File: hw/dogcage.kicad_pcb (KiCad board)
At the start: 2 copper layers, 68.6 x 49.8 mm, 17 parts, among them CON1 5V, M1 XBee, P1 Door, P2 Servo, P3 CONN_01X10, P4 CONN_01X10, P5 CONN_01X14, P7 CONN_01X14, Q1 TIP120, SW1 Trigger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

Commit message: Placement in progress
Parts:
- removed M1: XBee, modules:xbee
- removed P3, P4: CONN_01X10, Pin_Headers:Pin_Header_Straight_1x10
- removed P5, P7: CONN_01X14, Pin_Headers:Pin_Header_Straight_1x14
- added C3: 10uF, Capacitors_SMD:C_0805_HandSoldering, F.Cu at (170.2, 170.9)
- added C4: 100uF, Capacitors_SMD:c_elec_3x5.3, F.Cu at (156.2, 161.8)
- added Q2: TIP120, Power_Integrations:TO-220, F.Cu at (166.6, 158.5)
- added R2: 10K, Resistors_SMD:R_0805_HandSoldering, F.Cu at (190.6, 134.1)
- added R3: 330, Resistors_SMD:R_0805_HandSoldering, F.Cu at (190.8, 124.3)
- added R4: 10K, Resistors_SMD:R_0805_HandSoldering, F.Cu at (190.8, 131.0)
- added R5: 470, Resistors_SMD:R_0805_HandSoldering, F.Cu at (170.2, 162.8)
- added R6: 470, Resistors_SMD:R_0805_HandSoldering, F.Cu at (170.2, 165.6)
- added SW2: SW_PUSH, Buttons_Switches_ThroughHole:SW_PUSH_SMALL, F.Cu at (153.4, 136.9)
- added U3: TEENSYLC, modules:Teensy-3.1, F.Cu at (192.2, 137.8)
- added U4: ESP-01v090, ESP8266:ESP-01, F.Cu at (184.7, 130.8)
- C1: value 10uF -> .1uF; footprint Capacitors_Elko_ThroughHole:Elko_vert_11x5mm_RM2 -> Capacitors_SMD:C_0805_HandSoldering
- C2: footprint Capacitors_Elko_ThroughHole:Elko_vert_11x5mm_RM2 -> Capacitors_SMD:C_0805_HandSoldering
- CON1: value 5V -> BARREL_JACK
- D1: value Assoc -> 1N4001; footprint LEDs:LED-3MM -> Diodes_ThroughHole:Diode_DO-41_SOD81_Horizontal_RM10
- D2: value 1N4001 -> Assoc LED; footprint Diodes_ThroughHole:Diode_DO-41_SOD81_Horizontal_RM10 -> LEDs:LED-0805
- P1: footprint Pin_Headers:Pin_Header_Straight_1x02 -> Pin_Headers:Pin_Header_Straight_1x03
- P2: value Servo -> Lock
- R1: value 330 -> 10K; footprint Resistors_ThroughHole:Resistor_Horizontal_RM10mm -> Resistors_SMD:R_0805_HandSoldering
- SW1: value Trigger -> SW_PUSH
- U1: value LD1117S33TR -> LD1117S50TR
- U2: value Teensy LC -> LD1117S33TR; footprint modules:Teensy-3.1 -> SMD_Packages:SOT-223
- moved U2 58.5 mm to (179.3, 171.2)
- moved SW1 49.2 mm to (153.1, 124.0), turned to 90 degrees
- moved D2 44.1 mm to (190.6, 120.7)
- moved R1 39.2 mm to (190.8, 128.2), turned to 180 degrees
- moved D1 32.1 mm to (186.2, 161.3), turned to 0 degrees
- moved P1 13.9 mm to (158.5, 167.9)
- moved C2 8.48 mm to (170.2, 173.5), turned to 180 degrees
- moved U1 6.61 mm to (179.3, 163.6)
- moved C1 4.50 mm to (170.2, 168.4), turned to 180 degrees
- moved Q1 3.05 mm to (164.3, 168.9), turned to 90 degrees
- moved P2 2.05 mm to (153.2, 167.9)
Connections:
- C1 pad 1: +5V -> VCC
- C2 pad 1: +3V3 -> +5V
- CON1 pad 3: Net-(CON1-Pad3) -> (no net)
- D1 pad 1: GND -> VCC
- D1 pad 2: Net-(D1-Pad2) -> Net-(CON1-Pad1)
- D2 pad 1: +5V -> Net-(D2-Pad1)
- D2 pad 2: Net-(CON1-Pad1) -> +3V3
- P1 pad 1: Net-(P1-Pad1) -> /D175V
- P1 pad 2: GND -> +5V
- P2 pad 1: Net-(P2-Pad1) -> /D175V
- Q1 pad 2: Net-(P2-Pad3) -> Net-(P1-Pad3)
- R1 pad 1: Net-(M1-Pad15) -> +3V3
- R1 pad 2: Net-(D1-Pad2) -> /D2
- SW1 pad 1: Net-(P5-Pad13) -> /D10
- U1 pad 2: +3V3 -> +5V
- U1 pad 3: +5V -> VCC
- U2 pad 2: Net-(P5-Pad2) -> +3V3
- U2 pad 3: Net-(P5-Pad3) -> +5V
- U2 pad 4: Net-(P5-Pad4) -> (no net)
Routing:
- net +5V: track 93.8 -> 0.00 mm, vias 4 -> 0
- net GND: track 52.6 -> 0.00 mm, vias 6 -> 0
- net Net-(M1-Pad15): track 51.5 -> 0.00 mm, vias 2 -> 0
- net +3V3: track 47.9 -> 0.00 mm, vias 1 -> 0
- net Net-(P5-Pad13): track 20.7 -> 0.00 mm
- net /XBEE_CTL: track 19.9 -> 0.00 mm
- net Net-(P1-Pad1): track 16.6 -> 0.00 mm
- net Net-(P2-Pad1): track 14.8 -> 0.00 mm
- net Net-(Q1-Pad1): track 14.3 -> 0.00 mm
- net Net-(P2-Pad3): track 11.7 -> 0.00 mm
- net Net-(CON1-Pad1): track 8.23 -> 0.00 mm
- net Net-(M1-Pad20): track 5.55 -> 0.00 mm
- net Net-(M1-Pad2): track 5.33 -> 0.00 mm
- net Net-(M1-Pad19): track 5.33 -> 0.00 mm
- net Net-(M1-Pad3): track 5.10 -> 0.00 mm
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- removed copper zone on B.Cu, net GND

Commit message: Placement is essentially done
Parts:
- removed SW1: SW_PUSH, Buttons_Switches_ThroughHole:SW_PUSH_SMALL
- added Activate: SW_PUSH, Buttons_Switches_ThroughHole:SW_PUSH_SMALL, F.Cu at (164.1, 170.7)
- CON1: value BARREL_JACK -> 6.5V+; footprint Connect:BARREL_JACK -> modules:BARREL_JACK-ROUND_TH
- Q1, Q2: value TIP120 -> Darl_NPN; footprint Power_Integrations:TO-220 -> SMD_Packages:DPAK-2; moved to B.Cu
- R5, R6: moved to B.Cu
- SW2: footprint Buttons_Switches_ThroughHole:SW_PUSH_SMALL -> Buttons_Switches_SMD:SW_SPST_FSMSM
- U3: value TEENSYLC -> Teensy LC
- U4: value ESP-01v090 -> ESP8266
- moved SW2 41.8 mm to (195.1, 133.6), turned to 270 degrees
- moved C4 15.0 mm to (171.2, 163.1), turned to 90 degrees
- moved P2 10.8 mm to (161.5, 161.0), turned to 90 degrees
- moved Q1 10.1 mm to (174.2, 170.8)
- moved Q2 9.06 mm to (174.4, 163.2), turned to 90 degrees
- moved D2 6.83 mm to (190.0, 127.5)
- moved U4 6.65 mm to (182.9, 137.2)
- moved R3 6.28 mm to (190.0, 130.6)
- moved R4 5.67 mm to (190.0, 136.7), turned to 180 degrees
- moved R2 5.62 mm to (190.0, 139.7), turned to 180 degrees
- moved R1 5.43 mm to (190.0, 133.6)
- moved R6 4.85 mm to (170.7, 170.4), turned to 90 degrees
- moved U3 4.53 mm to (191.5, 142.2)
- moved P1 4.49 mm to (161.5, 164.6), turned to 90 degrees
- moved C1 1.27 mm to (171.2, 167.6)
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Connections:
- Q1 pad 1: Net-(Q1-Pad1) -> GND
- Q1 pad 2: Net-(P1-Pad3) -> Net-(Q1-Pad2)
- Q1 pad 3: GND -> Net-(P1-Pad3)
- Q2 pad 1: Net-(Q2-Pad1) -> GND
- Q2 pad 2: Net-(P2-Pad3) -> Net-(Q2-Pad2)
- Q2 pad 3: GND -> Net-(P2-Pad3)
- R5 pad 1: /D11 -> /D14
- R5 pad 2: Net-(Q1-Pad1) -> Net-(Q1-Pad2)
- R6 pad 1: /D12 -> /D15
- R6 pad 2: Net-(Q2-Pad1) -> Net-(Q2-Pad2)
- U3 pad 13: /D11 -> (no net)
- U3 pad 14: /D12 -> (no net)
- U3 pad 21: (no net) -> /D14
- U3 pad 22: (no net) -> /D15
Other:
- board size 68.6 x 49.8 mm -> 40.6 x 49.8 mm
- board text added: "Tom Manley tom.manley@gmail.com https://github.com/tpmanley/dogcage Version 2.0"
- board text removed: "https://github.com/tpmanley/dogcage Tom Manley tom.manley@gmail.com"

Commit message: Partially routed
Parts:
- removed Activate: SW_PUSH, Buttons_Switches_ThroughHole:SW_PUSH_SMALL
- added SW1: Activate, Buttons_Switches_ThroughHole:SW_PUSH_SMALL, F.Cu at (163.8, 170.9)
- moved R1 5.59 mm to (190.0, 139.2)
- moved R2 3.30 mm to (190.0, 136.4)
- moved R4 2.79 mm to (190.0, 133.9)
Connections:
- U3 pad 12: /D10 -> (no net)
- U3 pad 19: (no net) -> Net-(SW1-Pad2)
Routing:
- net +3V3: track 0.00 -> 97.9 mm, vias 0 -> 4
- net +5V: track 0.00 -> 41.1 mm, vias 0 -> 1
- net /TX1: track 0.00 -> 24.1 mm
- net Net-(CON1-Pad1): track 0.00 -> 22.9 mm
- net /D175V: track 0.00 -> 22.2 mm
- net VCC: track 0.00 -> 21.7 mm
- net /D2: track 0.00 -> 19.2 mm
- net Net-(R3-Pad2): track 0.00 -> 17.1 mm
- net Net-(SW1-Pad2): track 0.00 -> 14.7 mm
- net /RX1: track 0.00 -> 12.2 mm
- net Net-(R4-Pad2): track 0.00 -> 6.50 mm
- net Net-(R2-Pad2): track 0.00 -> 6.50 mm
- net Net-(D2-Pad1): track 0.00 -> 3.17 mm
- net Net-(P1-Pad3): track 0.00 -> 1.40 mm
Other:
- net class Power added: clearance 0.2, trace_width 0.762, via_dia 0.6858, via_drill 0.3302

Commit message: More routing
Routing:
- net +5V: track 41.1 -> 47.7 mm
- net Net-(P1-Pad3): track 1.40 -> 3.84 mm
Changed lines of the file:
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@@
   (general
     (links 49)
-    (no_connects 24)
+    (no_connects 23)
     (area 155.19281 124.351 201.577621 175.310001)
     (thickness 1.6)
     (drawings 5)
-    (tracks 100)
+    (tracks 108)
     (zones 0)
     (modules 23)
@@
     (pad_to_mask_clearance 0)
     (aux_axis_origin 0 0)
-    (visible_elements FFFF7B7F)
+    (visible_elements FFFFFF7F)
     (pcbplotparams
       (layerselection 0x010f0_80000001)
@@
   )
   (gr_line (start 198.12 125.476) (end 198.12 175.26) (angle 90) (layer Edge.Cuts) (width 0.1))
-  (segment (start 171.196 161.56686) (end 171.196 160.274) (width 0.762) (layer F.Cu) (net 1))
-  (segment (start 171.196 160.274) (end 171.196 159.258) (width 0.762) (layer B.Cu) (net 1))
-  (via (at 171.196 160.274) (size 0.6858) (layers F.Cu B.Cu) (net 1))
+  (segment (start 171.196 161.56686) (end 171.196 161.544) (width 0.508) (layer F.Cu) (net 1))
+  (segment (start 171.196 161.544) (end 169.799 160.147) (width 0.508) (layer F.Cu) (net 1))
+  (segment (start 169.799 160.147) (end 169.799 159.004) (width 0.508) (layer B.Cu) (net 1))
+  (via (at 169.799 160.147) (size 0.6858) (layers F.Cu B.Cu) (net 1))
+  (segment (start 168.656 159.004) (end 169.799 159.004) (width 0.508) (layer B.Cu) (net 1))
+  (segment (start 169.799 159.004) (end 192.532 159.004) (width 0.508) (layer B.Cu) (net 1))
+  (segment (start 192.532 159.004) (end 194.056 157.48) (width 0.508) (layer B.Cu) (net 1))
+  (segment (start 166.116 159.004) (end 164.084 161.036) (width 0.508) (layer B.Cu) (net 1))
+  (segment (start 168.656 159.004) (end 166.116 159.004) (width 0.508) (layer B.Cu) (net 1))
+  (segment (start 171.196 161.56686) (end 172.99686 161.56686) (width 0.762) (layer F.Cu) (net 1))
+  (segment (start 172.99686 161.56686) (end 175.006 163.576) (width 0.762) (layer F.Cu) (net 1))
+  (segment (start 175.006 163.576) (end 176.022 163.576) (width 0.762) (layer F.Cu) (net 1))
   (segment (start 164.084 161.036) (end 164.084 160.782) (width 0.762) (layer B.Cu) (net 1))
-  (segment (start 164.084 160.782) (end 165.608 159.258) (width 0.762) (layer B.Cu) (net 1))
-  (segment (start 192.278 159.258) (end 194.056 157.48) (width 0.762) (layer B.Cu) (net 1))
-  (segment (start 165.608 159.258) (end 171.196 159.258) (width 0.762) (layer B.Cu) (net 1))
-  (segment (start 171.196 159.258) (end 192.278 159.258) (width 0.762) (layer B.Cu) (net 1))
   (segment (start 164.084 161.036) (end 164.084 164.592) (width 0.762) (layer B.Cu) (net 1))
   (segment (start 172.7 173.482) (end 172.446 173.736) (width 0.762) (layer F.Cu) (net 1))
   (segment (start 176.022 173.482) (end 172.7 173.482) (width 0.762) (layer F.Cu) (net 1))
-  (segment (start 172.446 169.184) (end 169.184 169.184) (width 0.762) (layer F.Cu) (net 3))
+  (segment (start 172.446 169.184) (end 169.184 169.184) (width 0.508) (layer F.Cu) (net 3))
+  (segment (start 169.184 169.184) (end 169.164 169.164) (width 0.508) (layer F.Cu) (net 3))
+  (via (at 169.164 169.164) (size 0.6858) (layers F.Cu B.Cu) (net 3))
+  (segment (start 168.91 165.354) (end 168.91 166.116) (width 0.508) (layer F.Cu) (net 3))
+  (segment (start 168.91 159.258) (end 172.158002 159.258) (width 0.508) (layer F.Cu) (net 3))
+  (segment (start 175.768 159.258) (end 179.07 159.258) (width 0.508) (layer F.Cu) (net 3))
+  (segment (start 181.102 159.258) (end 183.134 159.258) (width 0.508) (layer F.Cu) (net 3))
+  (segment (start 184.912 159.258) (end 187.706 159.258) (width 0.508) (layer F.Cu) (net 3))
+  (segment (start 196.342 154.178) (end 196.342 159.258) (width 0.508) (layer F.Cu) (net 3))
+  (segment (start 192.532 139.192) (end 193.802 140.462) (width 0.508) (layer F.Cu) (net 3))
+  (segment (start 193.802 140.462) (end 195.072 140.462) (width 0.508) (layer F.Cu) (net 3))
+  (segment (start 195.072 140.462) (end 196.342 141.732) (width 0.508) (layer F.Cu) (net 3))
+  (segment (start 196.342 141.732) (end 196.342 154.178) (width 0.508) (layer F.Cu) (net 3))
+  (segment (start 192.532 139.192) (end 191.342 139.192) (width 0.508) (layer F.Cu) (net 3))
+  (segment (start 196.342 159.258) (end 189.484 159.258) (width 0.508) (layer F.Cu) (net 3))
+  (segment (start 187.706 159.258) (end 189.484 159.258) (width 0.508) (layer F.Cu) (net 3))
+  (segment (start 183.134 159.258) (end 184.912 159.258) (width 0.508) (layer F.Cu) (net 3))
+  (segment (start 179.07 159.258) (end 181.102 159.258) (width 0.508) (layer F.Cu) (net 3))
+  (segment (start 172.158002 159.258) (end 175.768 159.258) (width 0.508) (layer F.Cu) (net 3))
+  (segment (start 168.91 159.258) (end 168.91 165.354) (width 0.508) (layer F.Cu) (net 3))
+  (segment (start 169.164 166.37) (end 169.164 169.164) (width 0.508) (layer B.Cu) (net 3))
+  (segment (start 168.91 166.116) (end 169.164 166.37) (width 0.508) (layer B.Cu) (net 3))
   (via (at 168.91 166.116) (size 0.6858) (layers F.Cu B.Cu) (net 3))
-  (segment (start 168.91 166.116) (end 169.164 166.37) (width 0.762) (layer B.Cu) (net 3))
-  (segment (start 169.164 166.37) (end 169.164 169.164) (width 0.762) (layer B.Cu) (net 3))
-  (segment (start 168.91 159.258) (end 168.91 165.354) (width 0.762) (layer F.Cu) (net 3))
-  (segment (start 172.158002 159.258) (end 175.768 159.258) (width 0.762) (layer F.Cu) (net 3))
-  (segment (start 179.07 159.258) (end 181.102 159.258) (width 0.762) (layer F.Cu) (net 3))
-  (segment (start 183.134 159.258) (end 184.912 159.258) (width 0.762) (layer F.Cu) (net 3))
-  (segment (start 187.706 159.258) (end 189.484 159.258) (width 0.762) (layer F.Cu) (net 3))
-  (segment (start 196.342 159.258) (end 189.484 159.258) (width 0.762) (layer F.Cu) (net 3))
-  (segment (start 192.532 139.192) (end 191.342 139.192) (width 0.762) (layer F.Cu) (net 3))
-  (segment (start 196.342 141.732) (end 196.342 154.178) (width 0.762) (layer F.Cu) (net 3))
-  (segment (start 195.072 140.462) (end 196.342 141.732) (width 0.762) (layer F.Cu) (net 3))
-  (segment (start 193.802 140.462) (end 195.072 140.462) (width 0.762) (layer F.Cu) (net 3))
-  (segment (start 192.532 139.192) (end 193.802 140.462) (width 0.762) (layer F.Cu) (net 3))
-  (segment (start 196.342 154.178) (end 196.342 159.258) (width 0.762) (layer F.Cu) (net 3))
-  (segment (start 184.912 159.258) (end 187.706 159.258) (width 0.762) (layer F.Cu) (net 3))
-  (segment (start 181.102 159.258) (end 183.134 159.258) (width 0.762) (layer F.Cu) (net 3))
-  (segment (start 175.768 159.258) (end 179.07 159.258) (width 0.762) (layer F.Cu) (net 3))
-  (segment (start 168.91 159.258) (end 172.158002 159.258) (width 0.762) (layer F.Cu) (net 3))
-  (segment (start 168.91 165.354) (end 168.91 166.116) (width 0.762) (layer F.Cu) (net 3))
-  (via (at 169.164 169.164) (size 0.6858) (layers F.Cu B.Cu) (net 3))
-  (segment (start 169.184 169.184) (end 169.164 169.164) (width 0.762) (layer F.Cu) (net 3))
   (segment (start 172.446 170.688) (end 172.446 169.184) (width 0.762) (layer F.Cu) (net 3))
   (segment (start 172.446 169.184) (end 172.466 169.164) (width 0.762) (layer F.Cu) (net 3))
@@
   (segment (start 175.514 170.688) (end 176.022 171.196) (width 0.762) (layer F.Cu) (net 3))
   (segment (start 172.446 170.688) (end 175.514 170.688) (width 0.762) (layer F.Cu) (net 3))
+  (segment (start 196.342 161.28746) (end 196.342 173.228) (width 0.508) (layer B.Cu) (net 4))
+  (segment (start 191.262 173.228) (end 196.342 173.228) (width 0.508) (layer B.Cu) (net 4))
+  (segment (start 191.262 173.228) (end 188.214 170.18) (width 0.508) (layer B.Cu) (net 4))
+  (segment (start 187.60186 170.18) (end 188.214 170.18) (width 0.508) (layer B.Cu) (net 4))
   (segment (start 196.596 161.54146) (end 196.342 161.28746) (width 0.254) (layer B.Cu) (net 4))
   (segment (start 187.60186 170.18) (end 187.96 170.18) (width 0.254) (layer B.Cu) (net 4))
   (segment (start 187.60186 170.58386) (end 187.60186 170.18) (width 0.762) (layer B.Cu) (net 4))
-  (segment (start 196.342 173.228) (end 190.246 173.228) (width 0.762) (layer B.Cu) (net 4))
-  (segment (start 190.246 173.228) (end 187.60186 170.58386) (width 0.762) (layer B.Cu) (net 4))
-  (segment (start 196.342 161.28746) (end 196.342 173.228) (width 0.762) (layer B.Cu) (net 4))
   (segment (start 174.244 167.64) (end 176.022 165.862) (width 0.762) (layer F.Cu) (net 6))
   (segment (start 172.446 167.64) (end 174.244 167.64) (width 0.762) (layer F.Cu) (net 6))
@@
   (segment (start 161.544 161.036) (end 159.004 158.496) (width 0.254) (layer B.Cu) (net 8))
   (segment (start 161.544 164.592) (end 161.544 161.036) (width 0.254) (layer B.Cu) (net 8))
+  (segment (start 168.529 164.592) (end 168.91 164.973) (width 0.508) (layer B.Cu) (net 9))
+  (segment (start 168.529 164.592) (end 166.624 164.592) (width 0.508) (layer B.Cu) (net 9))
   (segment (start 174.244 168.529) (end 172.847 168.529) (width 0.254) (layer B.Cu) (net 9))
   (segment (start 178.816 139.192) (end 178.562 138.938) (width 0.254) (layer F.Cu) (net 10))

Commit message: Everything connected except GND
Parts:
- moved R6 7.55 mm to (172.3, 163.1), turned to 0 degrees
- moved R5 7.55 mm to (172.1, 170.8), turned to 0 degrees
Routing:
- net /D14: track 0.00 -> 19.2 mm, vias 0 -> 1
- net /D15: track 0.00 -> 9.12 mm, vias 0 -> 1
- net Net-(P2-Pad3): track 0.00 -> 7.80 mm
- net Net-(SW1-Pad2): track 14.7 -> 22.3 mm
- net Net-(Q1-Pad2): track 0.00 -> 7.16 mm
- net Net-(Q2-Pad2): track 0.00 -> 7.08 mm
- net Net-(P1-Pad3): track 3.84 -> 10.6 mm
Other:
- net class Power: trace_width 0.762 -> 0.508

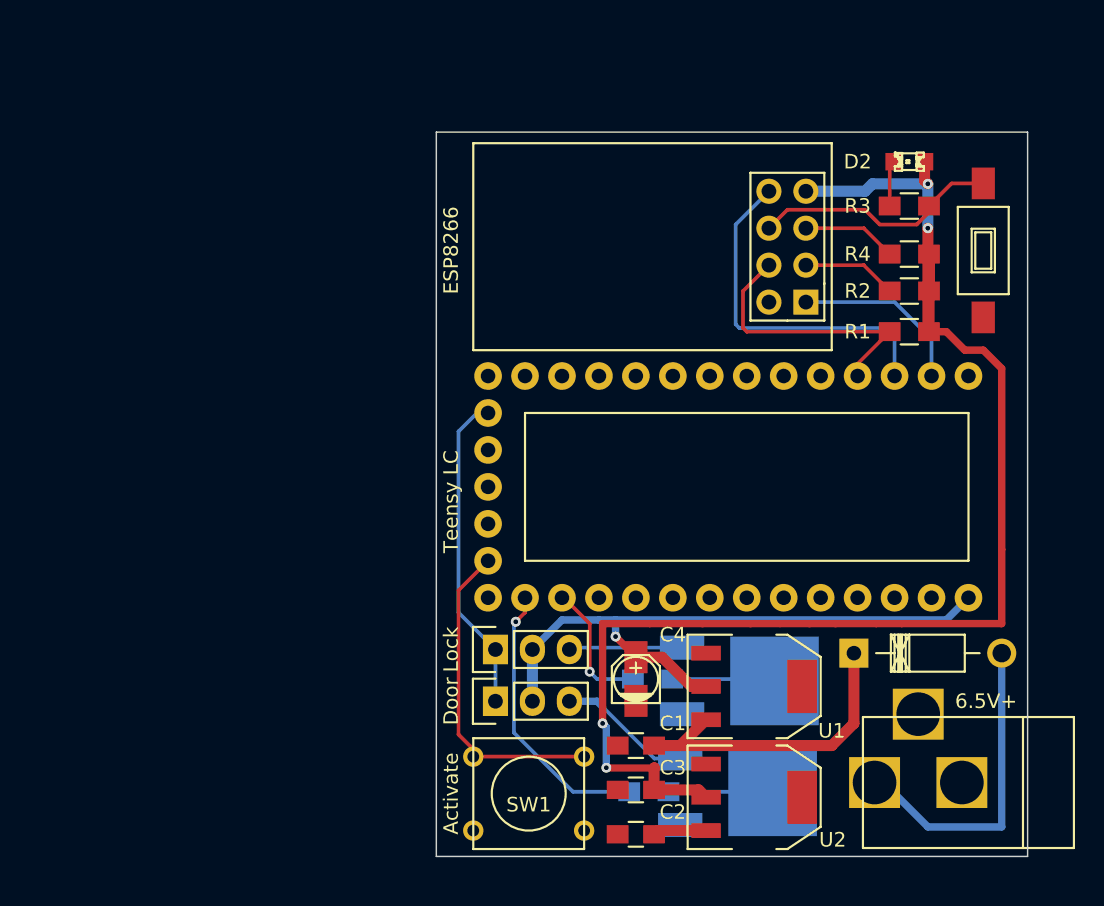
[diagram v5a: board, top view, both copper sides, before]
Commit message: Almost made all GND connections
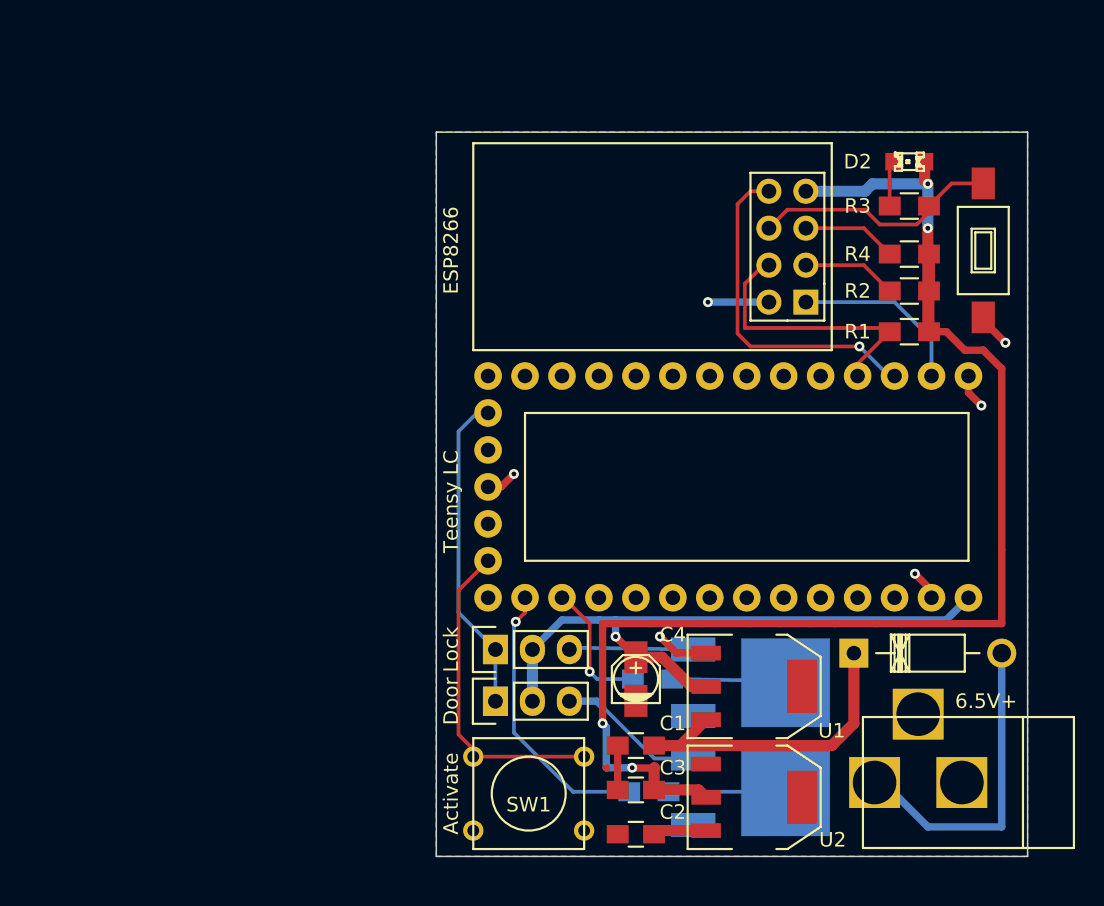
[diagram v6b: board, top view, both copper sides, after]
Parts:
- moved Q1 0.89 mm to (175.1, 170.8)
- moved Q2 0.77 mm to (175.1, 163.3)
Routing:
- net GND: track 0.00 -> 19.9 mm, vias 0 -> 6
- net Net-(P1-Pad3): track 10.6 -> 11.5 mm
- net Net-(Q1-Pad2): track 7.16 -> 8.05 mm
- net Net-(Q2-Pad2): track 7.08 -> 7.85 mm
- net Net-(P2-Pad3): track 7.80 -> 8.56 mm
- net /TX1: track 24.1 -> 24.8 mm, vias 0 -> 1
- added copper zone on B.Cu, net GND
- added copper zone on F.Cu, net GND
